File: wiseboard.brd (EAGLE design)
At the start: 80 x 55 mm, 102 parts, among them IC1 MCP73871-2CCI/ML-ND, IC2 LM358MX, Q1 IRLML6402TRPBF, Q2 IRLML6402TRPBF, U1 LT1945EMSPBF, X1 1528-1438-ND

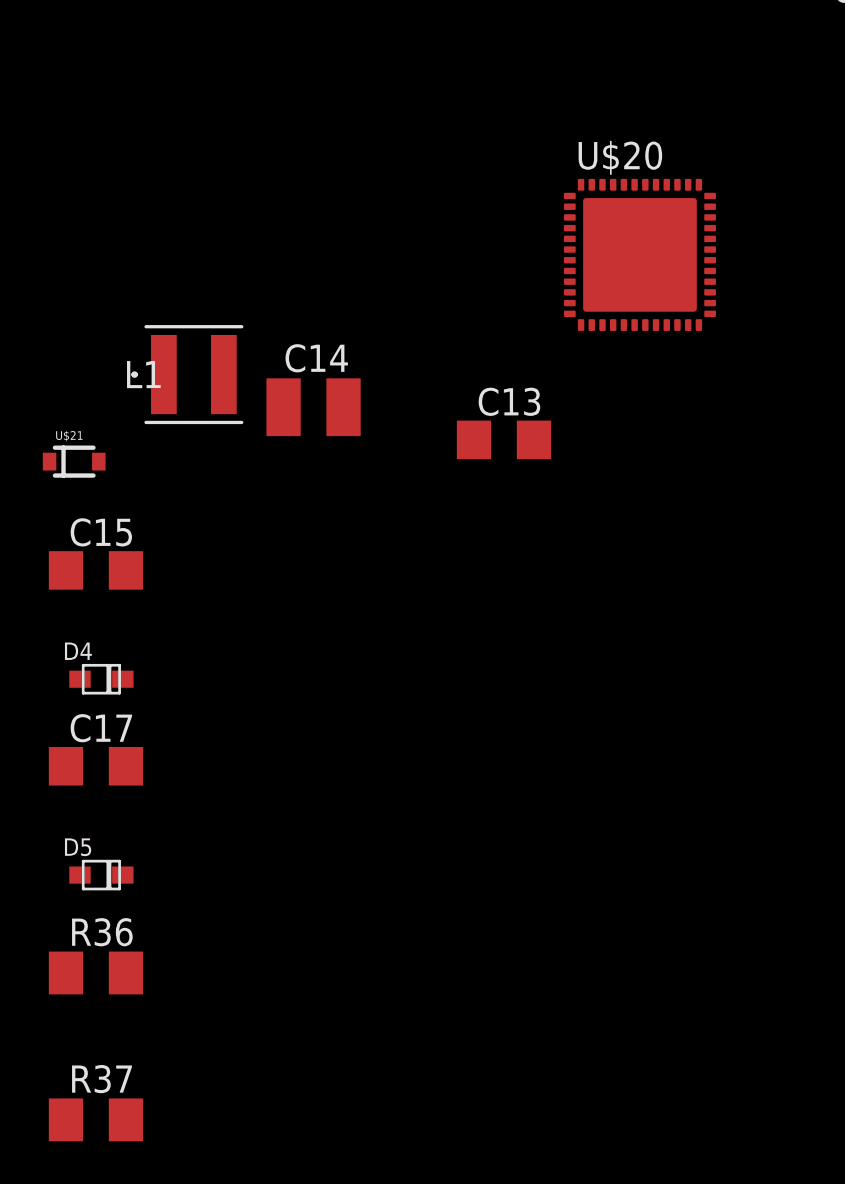
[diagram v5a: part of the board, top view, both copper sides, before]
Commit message: Revert "ADD NEW POWER SUPPLY CHIP AND UPDATED WISE LIB"
This reverts commit 5b119768b8ee24b661b8f63ccc7bfa2b79d5fd4d.
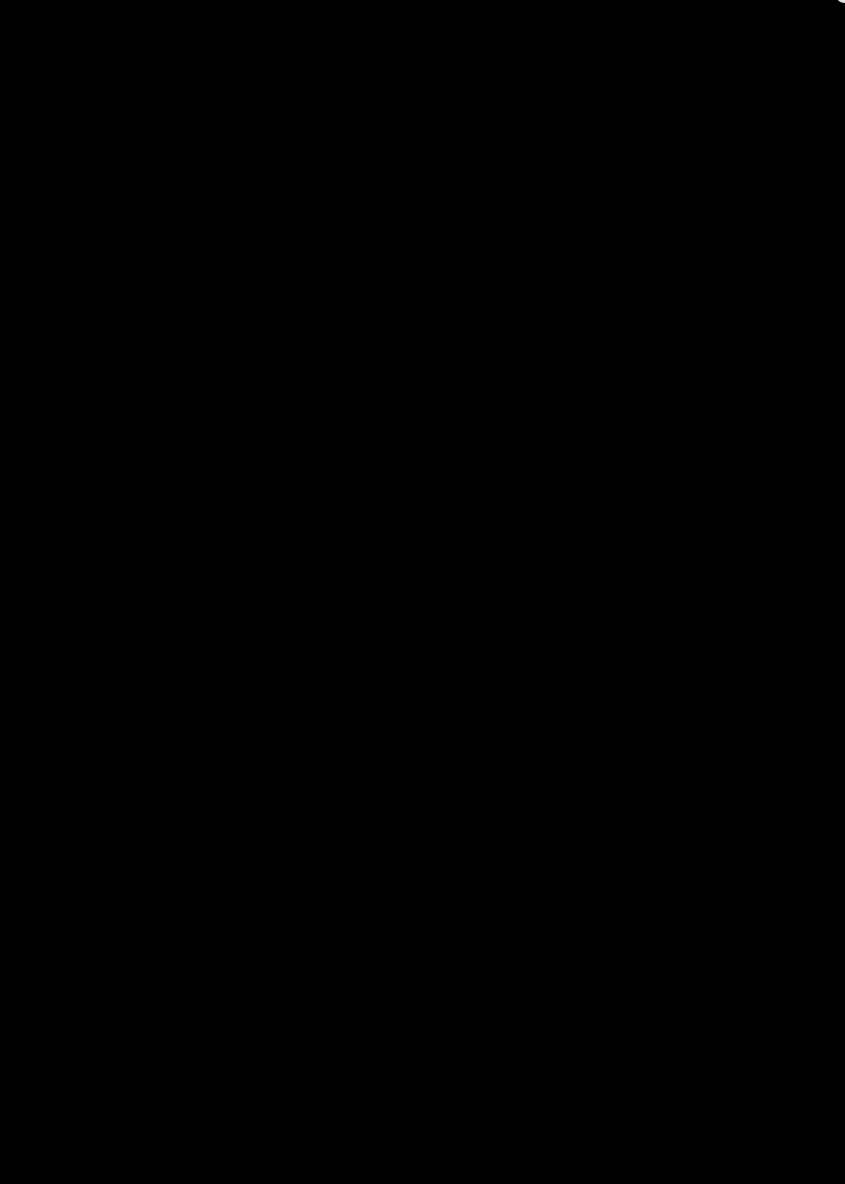
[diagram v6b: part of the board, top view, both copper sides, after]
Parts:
- removed C13: 4u7F, adafruit:C1206
- removed C14: 10uF, adafruit:C1210
- removed C15: 100nF, adafruit:C1206
- removed C17: 10nF, adafruit:C1206
- removed D4, D5: (no value), adafruit:SOD-323F
- removed L1: NR4012T2R2M, WISE:NR4012T2R2M
- removed R36, R37: 470k, adafruit:M1206
- removed U$20: TPS65186, WISE:QFN48
- removed U$21: BAS3010, WISE:SOD-323
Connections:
- removed net N$17: L1.2, U$20.40, U$21.2
- removed net N$28: C13.2, U$20.37, U$20.42, U$21.1
- removed net N$30: C15.2, D4.A, U$20.35
- removed net N$32: C17.1, D4.C, D5.A
- removed net N$34: C17.2, U$20.36
- removed net N$36: D5.C, R36.2
- removed net N$37: U$20.34
- net GND: no longer C13.1, C14.1, C15.1, U$20.41
- net VBAT: no longer C14.2, L1.1
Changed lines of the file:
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@@
 <element name="IC2" library="linear" library_urn="urn:adsk.eagle:library:262" package="SO08" value="LM358MX" x="33.147" y="41.148" rot="R90"/>
 <element name="CN1" library="adafruit" package="JST-PH-2-SMT-RA" value="" x="4.572" y="3.556" rot="R180"/>
-<element name="U$20" library="WISE" package="QFN48" value="TPS65186" x="7.62" y="-13.462"/>
-<element name="C13" library="adafruit" package="C1206" value="4u7F" x="1.27" y="-22.098"/>
-<element name="C14" library="adafruit" package="C1210" value="10uF" x="-7.62" y="-20.574"/>
-<element name="L1" library="WISE" package="NR4012T2R2M" value="NR4012T2R2M" x="-13.208" y="-19.05">
-<attribute name="MANUFACTURER_PART_NUMBER" value="NR4012T2R2M" x="-13.208" y="-19.05" size="1.778" layer="27" display="off"/>
-<attribute name="VENDOR" value="Taiyo Yuden" x="-13.208" y="-19.05" size="1.778" layer="27" display="off"/>
-</element>
-<element name="U$21" library="WISE" package="SOD-323" value="BAS3010" x="-18.796" y="-23.114"/>
-<element name="C15" library="adafruit" package="C1206" value="100nF" x="-17.78" y="-28.194"/>
-<element name="D4" library="adafruit" package="SOD-323F" value="" x="-17.526" y="-33.274"/>
-<element name="C17" library="adafruit" package="C1206" value="10nF" x="-17.78" y="-37.338"/>
-<element name="D5" library="adafruit" package="SOD-323F" value="" x="-17.526" y="-42.418"/>
-<element name="R36" library="adafruit" package="M1206" value="470k" x="-17.78" y="-46.99"/>
-<element name="R37" library="adafruit" package="M1206" value="470k" x="-17.78" y="-53.848"/>
 </elements>
 <signals>
@@
 <wire x1="10.506175" y1="10.5184" x2="14.8876" y2="10.5184" width="0.1524" layer="1"/>
 <wire x1="14.8876" y1="10.5184" x2="15.008" y2="10.398" width="0.1524" layer="1"/>
-<contactref element="C13" pad="1"/>
-<contactref element="C14" pad="1"/>
-<contactref element="U$20" pad="41"/>
-<contactref element="C15" pad="1"/>
-<wire x1="57.429" y1="32.5685" x2="75.695" y2="20.32" width="0" layer="19" extent="1-1"/>
-<wire x1="55.245" y1="29.0195" x2="57.429" y2="32.5685" width="0" layer="19" extent="1-1"/>
-<wire x1="49.5935" y1="33.274" x2="55.245" y2="29.0195" width="0" layer="19" extent="1-1"/>
-<wire x1="47.6826" y1="35.2366" x2="49.5935" y2="33.274" width="0" layer="19" extent="1-1"/>
+<wire x1="20.574" y1="37.846" x2="22.2885" y2="36.5125" width="0" layer="19" extent="1-1"/>
 <wire x1="43.688" y1="36.068" x2="43.5776" y2="33.6384" width="0" layer="19" extent="16-16"/>
-<wire x1="27.746" y1="40.513" x2="31.2308125" y2="36.0121" width="0" layer="19" extent="1-1"/>
-<wire x1="27.746" y1="41.783" x2="27.746" y2="40.513" width="0" layer="19" extent="1-1"/>
-<wire x1="22.546" y1="41.783" x2="27.746" y2="41.783" width="0" layer="19" extent="1-1"/>
-<wire x1="22.546" y1="40.513" x2="22.546" y2="41.783" width="0" layer="19" extent="1-1"/>
-<wire x1="20.574" y1="37.846" x2="22.546" y2="40.513" width="0" layer="19" extent="1-1"/>
-<wire x1="22.2885" y1="36.5125" x2="20.574" y2="37.846" width="0" layer="19" extent="1-1"/>
-<wire x1="23.3045" y1="35.7759" x2="22.2885" y2="35.7759" width="0" layer="19" extent="1-1"/>
+<wire x1="49.5935" y1="33.274" x2="47.6826" y2="35.2366" width="0" layer="19" extent="1-1"/>
 <wire x1="22.7965" y1="31.4071" x2="18.9808" y2="31.496" width="0" layer="19" extent="1-16"/>
 <wire x1="30.858" y1="22.479" x2="30.731" y2="25.273" width="0" layer="19" extent="1-1"/>
+<wire x1="27.746" y1="40.513" x2="22.546" y2="40.513" width="0" layer="19" extent="1-1"/>
+<wire x1="7.112" y1="43.825" x2="11.079" y2="43.942" width="0" layer="19" extent="1-1"/>
 <wire x1="30.48" y1="17.015" x2="30.858" y2="22.479" width="0" layer="19" extent="1-1"/>
 <wire x1="25.397" y1="16.256" x2="30.48" y2="17.015" width="0" layer="19" extent="1-1"/>
 <wire x1="22.733" y1="16.8025" x2="25.397" y2="16.256" width="0" layer="19" extent="1-1"/>
+<wire x1="29.0322" y1="50.7746" x2="33.3248" y2="46.2534" width="0" layer="19" extent="1-1"/>
 <wire x1="28.448" y1="10.6015" x2="25.397" y2="16.256" width="0" layer="19" extent="1-1"/>
 <wire x1="34.147" y1="10.065" x2="28.448" y2="10.6015" width="0" layer="19" extent="1-1"/>
-<wire x1="35.147" y1="11.065" x2="34.147" y2="10.065" width="0" layer="19" extent="1-1"/>
 <wire x1="37.973" y1="10.77" x2="35.147" y2="11.065" width="0" layer="19" extent="1-1"/>
 <wire x1="40.259" y1="10.77" x2="37.973" y2="10.77" width="0" layer="19" extent="1-1"/>
 <wire x1="40.259" y1="4.674" x2="40.259" y2="10.77" width="0" layer="19" extent="1-1"/>
-<wire x1="42.545" y1="4.674" x2="40.259" y2="4.674" width="0" layer="19" extent="1-1"/>
 <wire x1="39.624" y1="16.9" x2="40.259" y2="10.77" width="0" layer="19" extent="1-1"/>
 <wire x1="42.418" y1="17.015" x2="39.624" y2="16.9" width="0" layer="19" extent="1-1"/>
-<wire x1="16.41475" y1="15.7226" x2="22.733" y2="16.8025" width="0" layer="19" extent="1-1"/>
-<wire x1="5.572" y1="7.256" x2="9.652" y2="10.414" width="0" layer="19" extent="1-16"/>
-<wire x1="14.986" y1="4.699" x2="15.008" y2="10.398" width="0" layer="19" extent="1-1"/>
-<wire x1="11.303" y1="2.159" x2="14.986" y2="4.699" width="0" layer="19" extent="1-1"/>
-<wire x1="16.002" y1="43.276" x2="19.304" y2="37.592" width="0" layer="19" extent="1-1"/>
-<wire x1="11.079" y1="43.942" x2="16.002" y2="43.276" width="0" layer="19" extent="1-1"/>
-<wire x1="11.306" y1="40.386" x2="11.079" y2="43.942" width="0" layer="19" extent="1-1"/>
-<wire x1="7.112" y1="43.825" x2="11.079" y2="43.942" width="0" layer="19" extent="1-1"/>
-<wire x1="3.2512" y1="38.811196875" x2="3.4483125" y2="37.9601" width="0" layer="19" extent="1-16"/>
-<wire x1="3.937" y1="41.81775" x2="5.588003125" y2="41.148" width="0" layer="19" extent="1-1"/>
-<wire x1="2.0645" y1="32.2255" x2="3.2512" y2="34.036" width="0" layer="19" extent="1-16"/>
-<wire x1="1.6575" y1="31.0255" x2="1.8281" y2="31.1961" width="0" layer="19" extent="1-1"/>
-<wire x1="1.6575" y1="29.2255" x2="1.6575" y2="31.0255" width="0" layer="19" extent="1-1"/>
-<wire x1="1.524" y1="41.81775" x2="3.937" y2="41.81775" width="0" layer="19" extent="1-1"/>
-<wire x1="1.6575" y1="22.6255" x2="1.6575" y2="29.2255" width="0" layer="19" extent="1-1"/>
-<wire x1="22.336" y1="7.256" x2="28.448" y2="10.6015" width="0" layer="19" extent="1-1"/>
-<wire x1="38.548" y1="43.053" x2="41.0408125" y2="36.4866" width="0" layer="19" extent="1-1"/>
-<wire x1="39.8272" y1="46.2534" x2="38.548" y2="43.053" width="0" layer="19" extent="1-1"/>
-<wire x1="43.561" y1="50.1015" x2="39.8272" y2="46.2534" width="0" layer="19" extent="1-1"/>
-<wire x1="33.3248" y1="46.2534" x2="38.548" y2="43.053" width="0" layer="19" extent="1-1"/>
-<wire x1="29.0322" y1="50.7746" x2="33.3248" y2="46.2534" width="0" layer="19" extent="1-1"/>
-<wire x1="22.5298" y1="50.7746" x2="29.0322" y2="50.7746" width="0" layer="19" extent="1-1"/>
-<wire x1="8.37" y1="-10.187" x2="11.303" y2="2.159" width="0" layer="19" extent="1-1"/>
-<wire x1="-0.13" y1="-22.098" x2="8.37" y2="-10.187" width="0" layer="19" extent="1-1"/>
-<wire x1="-9.02" y1="-20.574" x2="-0.13" y2="-22.098" width="0" layer="19" extent="1-1"/>
-<wire x1="-19.18" y1="-28.194" x2="-9.02" y2="-20.574" width="0" layer="19" extent="1-1"/>
+<wire x1="55.245" y1="29.0195" x2="49.5935" y2="33.274" width="0" layer="19" extent="1-1"/>
 </signal>
 <signal name="VCC">
@@
 <via x="20.75" y="33.5" extent="1-16" drill="0.508"/>
 <via x="25.75" y="28.5" extent="1-16" drill="0.508"/>
-<contactref element="L1" pad="1"/>
-<contactref element="C14" pad="2"/>
-<wire x1="-6.22" y1="-20.574" x2="-14.608" y2="-19.05" width="0" layer="19" extent="1-1"/>
-<wire x1="5" y1="4.625" x2="-6.22" y2="-20.574" width="0" layer="19" extent="1-1"/>
 </signal>
 <signal name="OE">
@@
 </polygon>
 </signal>
-<signal name="N$17">
-<contactref element="U$20" pad="40"/>
-<contactref element="L1" pad="2"/>
-<contactref element="U$21" pad="2"/>
-<wire x1="-11.808" y1="-19.05" x2="-17.646" y2="-23.114" width="0" layer="19" extent="1-1"/>
-<wire x1="8.87" y1="-10.187" x2="-11.808" y2="-19.05" width="0" layer="19" extent="1-1"/>
-</signal>
-<signal name="N$28">
-<contactref element="U$21" pad="1"/>
-<contactref element="C13" pad="2"/>
-<contactref element="U$20" pad="42"/>
-<contactref element="U$20" pad="37"/>
-<wire x1="2.67" y1="-22.098" x2="-19.946" y2="-23.114" width="0" layer="19" extent="1-1"/>
-<wire x1="7.87" y1="-10.187" x2="2.67" y2="-22.098" width="0" layer="19" extent="1-1"/>
-<wire x1="10.37" y1="-10.187" x2="7.87" y2="-10.187" width="0" layer="19" extent="1-1"/>
-</signal>
-<signal name="N$30">
-<contactref element="U$20" pad="35"/>
-<contactref element="C15" pad="2"/>
-<contactref element="D4" pad="A"/>
-<wire x1="-16.38" y1="-28.194" x2="-18.526" y2="-33.274" width="0" layer="19" extent="1-1"/>
-<wire x1="10.895" y1="-11.212" x2="-16.38" y2="-28.194" width="0" layer="19" extent="1-1"/>
-</signal>
-<signal name="N$32">
-<contactref element="D4" pad="C"/>
-<contactref element="C17" pad="1"/>
-<contactref element="D5" pad="A"/>
-<wire x1="-19.18" y1="-37.338" x2="-18.526" y2="-42.418" width="0" layer="19" extent="1-1"/>
-<wire x1="-16.526" y1="-33.274" x2="-19.18" y2="-37.338" width="0" layer="19" extent="1-1"/>
-</signal>
-<signal name="N$34">
-<contactref element="U$20" pad="36"/>
-<contactref element="C17" pad="2"/>
-<wire x1="10.895" y1="-10.712" x2="-16.38" y2="-37.338" width="0" layer="19" extent="1-1"/>
-</signal>
-<signal name="N$36">
-<contactref element="D5" pad="C"/>
-<contactref element="R36" pad="2"/>
-<wire x1="-16.526" y1="-42.418" x2="-16.38" y2="-46.99" width="0" layer="19" extent="1-1"/>
-</signal>
-<signal name="N$37">
-<contactref element="U$20" pad="34"/>
-</signal>
 </signals>

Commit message: CONTINUE ROUTING REV1 PCB BOARD
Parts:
- moved R31 3.64 mm to (75.1, 2.16)
- moved R30 2.75 mm to (76.6, 18.7)
- moved R35 2.75 mm to (76.6, 21.8)
- moved R33 1.55 mm to (58.8, 18.7)
- moved INPUTBUTTONHEADER1 1.05 mm to (56.8, 22.0)
- moved S4 0.40 mm to (74.5, 12.2), turned to 270 degrees
- moved S6 0.18 mm to (58.5, 12.2), turned to 90 degrees
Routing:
- net VCOMMON: track 20.7 -> 79.8 mm, vias 2 -> 8
- net N$26: track 140.4 -> 173.2 mm, vias 5 -> 7
- net GND: track 118.1 -> 146.2 mm, vias 20 -> 22
- net +3V3: track 216.4 -> 237.6 mm, vias 5 -> 9
- net N$33: track 9.14 -> 13.0 mm, vias 0 -> 1
- net ADC: track 68.7 -> 71.0 mm, vias 5 -> 6
- net +22V: track 157.1 -> 158.1 mm
- net N$3: track 69.9 -> 70.9 mm
- net +15V: track 71.7 -> 72.6 mm
- net RESET: track 80.2 -> 80.9 mm
- net N$29: track 16.2 -> 16.0 mm, vias 0 -> 1

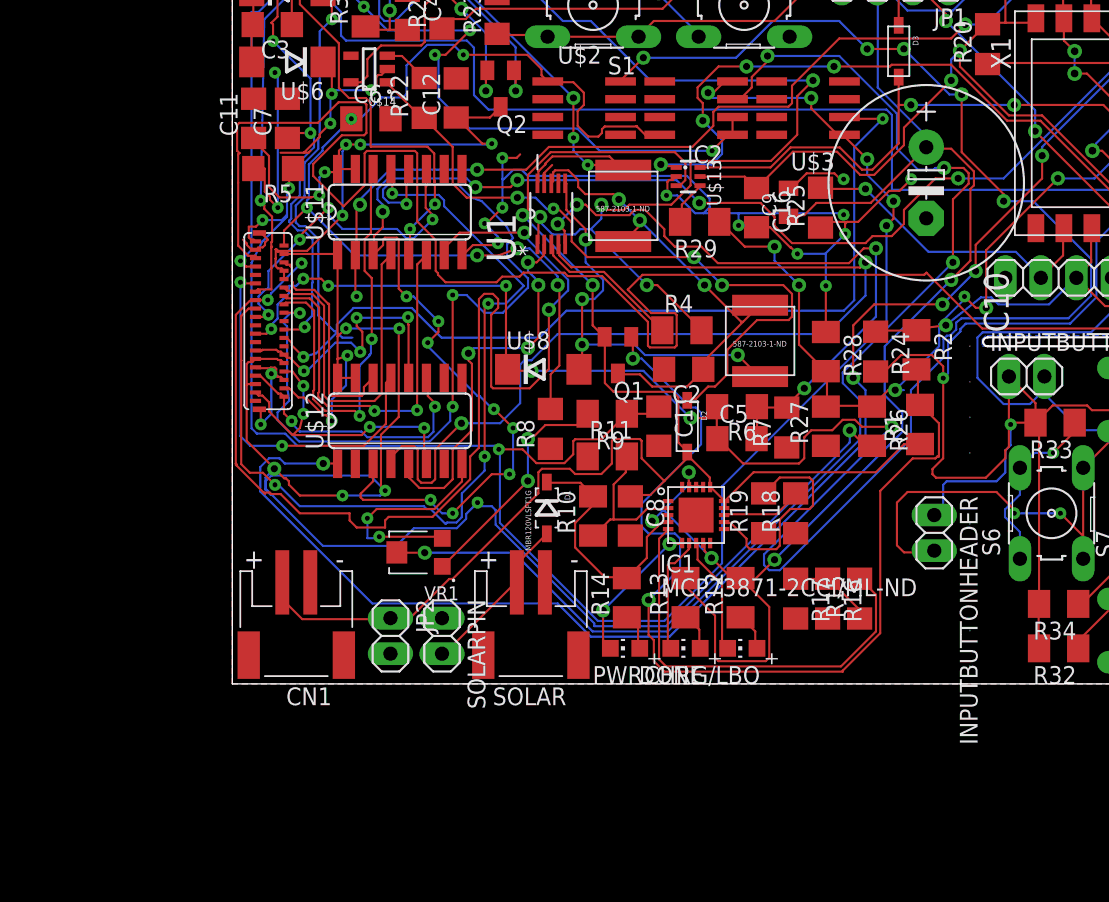
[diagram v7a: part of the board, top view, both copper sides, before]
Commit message: CONTINUED MODIFYING SOLAR CHARGER
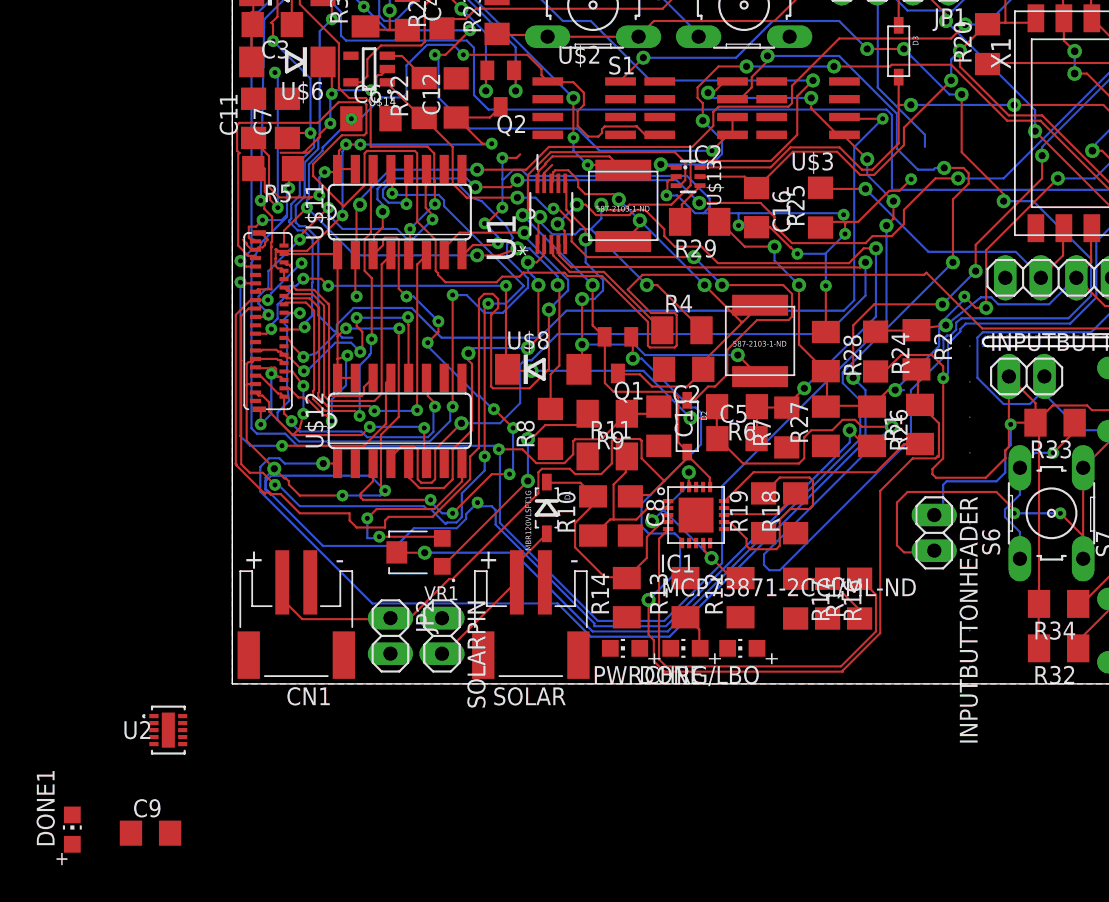
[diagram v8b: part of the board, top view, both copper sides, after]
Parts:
- removed C10: 4700uF/10V, adafruit:E5-13
- added DONE1: GREEN, adafruit:CHIP-LED0805
- added U2: BQ24210DQCT, WISE:DQC10_P84X2P4
- C9: value 10uF/10V -> 2u2F; device adafruit:C0805K -> adafruit:C1206
- moved C9 64.1 mm to (-5.84, -10.7), turned to 0 degrees
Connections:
- new net VBAT1: IC1.14
- new net VBAT2: IC1.15
- new net VBAT3: IC1.16
- net GND: now also DONE.C, U2.11, U2.3; no longer C10.-
- net N$10: now also CHRG/LBO.C, R14.1; no longer IC1.6, PWR.C
- net N$11: now also PWR.A, R12.2; no longer DONE.C, IC1.7
- net N$13: now also C9.1, D1.C, U2.1; no longer CHRG/LBO.A, R12.1
- net N$15: now also R13.2, R14.2, U2.8; no longer PWR.A, R14.1
- net N$16: now also DONE1.C, U2.6; no longer CHRG/LBO.C, IC1.8
- net VBAT: now also CHRG/LBO.A, DONE1.A, U2.10; no longer IC1.14, IC1.15, IC1.16
- net VCC: no longer C10.+, C9.1, D1.C, R12.2, R13.2, R14.2
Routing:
- net VCC: track 119.5 -> 47.7 mm, vias 5 -> 3
- net N$10: track 10.6 -> 0.00 mm, vias 2 -> 0
- net N$16: track 8.47 -> 0.00 mm
- net N$11: track 8.46 -> 0.00 mm
- net GND: track 146.2 -> 141.6 mm, vias 22 -> 21
- net N$13: track 2.74 -> 0.00 mm
- net N$15: track 2.64 -> 0.00 mm
- net VBAT: track 106.8 -> 104.6 mm
